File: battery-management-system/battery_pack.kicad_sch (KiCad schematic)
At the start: 16 parts, among them J1 CELL4_PLUS, J2 CELL4_MINUS, J3 CELL3_MINUS, J4 CELL2_MINUS, J5 CELL1_MINUS, J6 VBAT+, J8 VBAT+, Q1 DMN3730U, Q2 TJ40S04M3L, Q3 TJ40S04M3L, Q4 DMN3730U

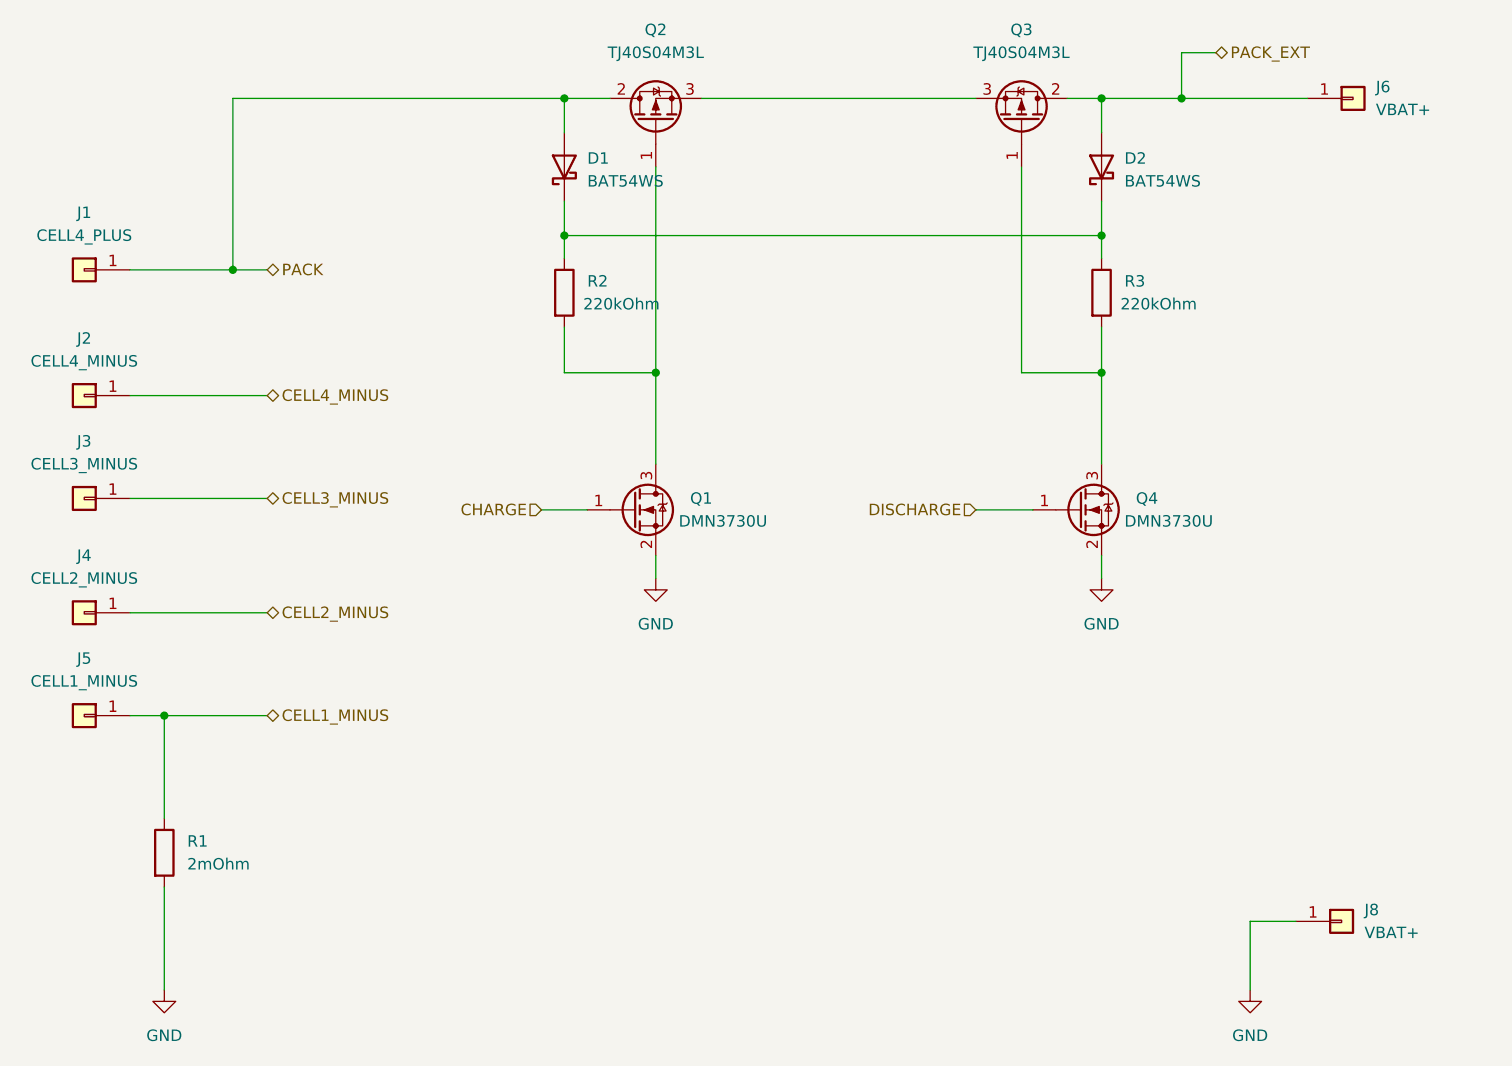
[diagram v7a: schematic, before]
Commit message: add resistors, capacitors and LEDs
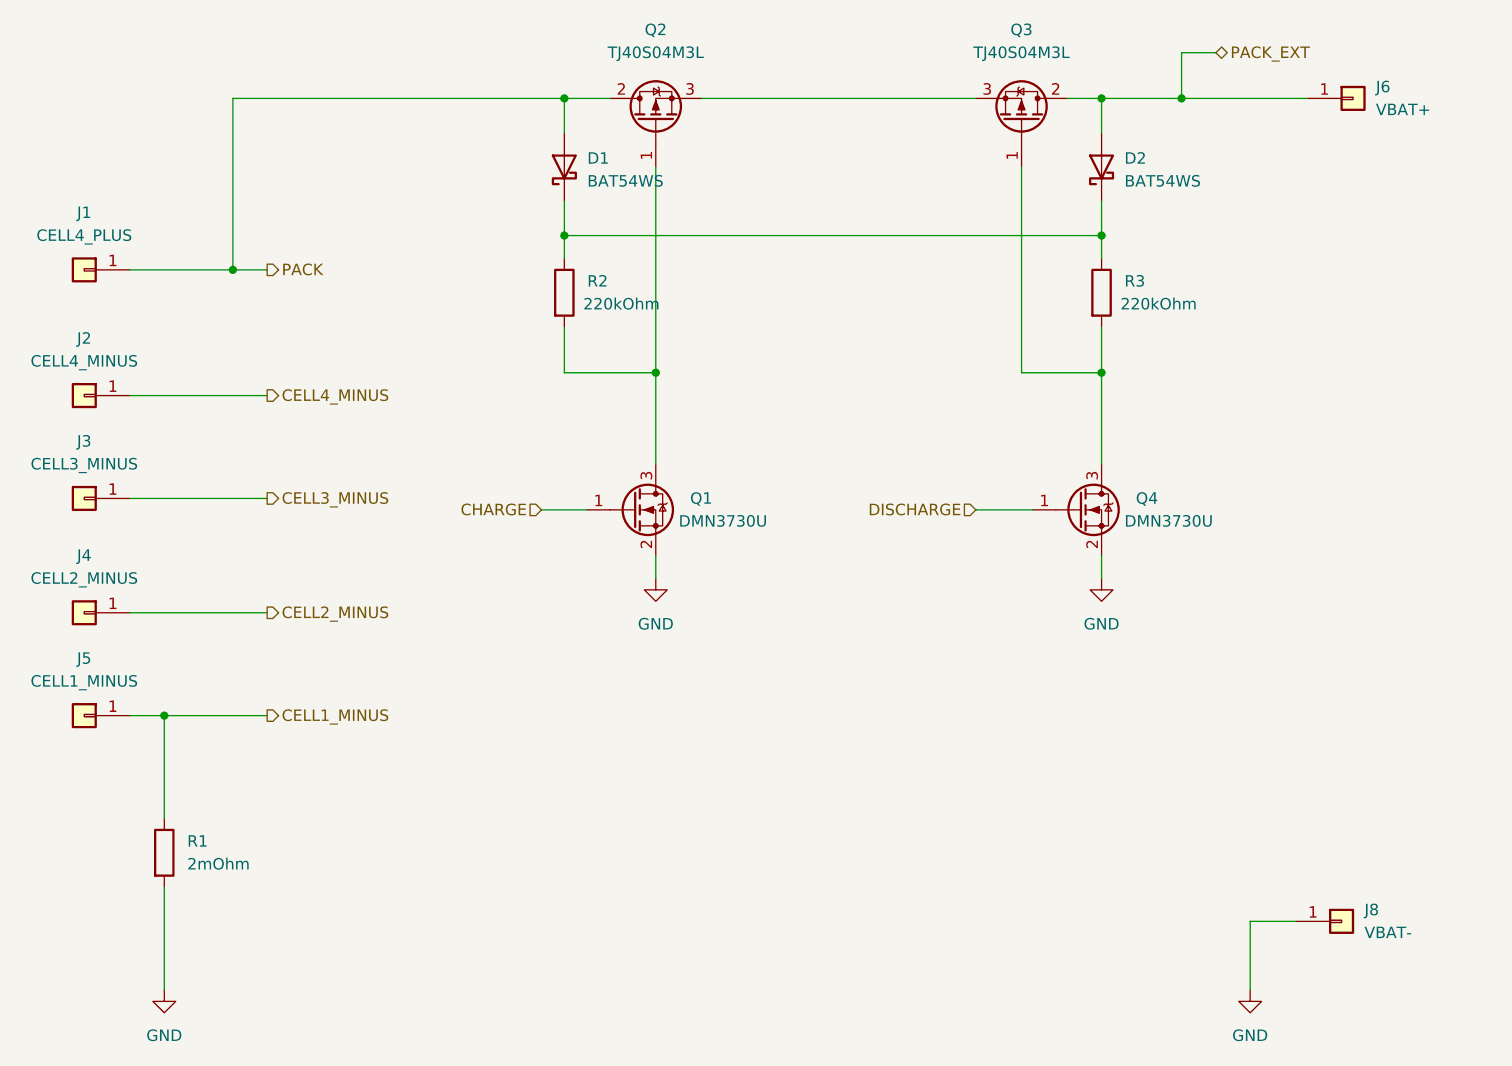
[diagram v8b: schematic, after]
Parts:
- J8: value VBAT+ -> VBAT-
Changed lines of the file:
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@@
     (effects (font (size 1.27 1.27)) (justify right))
   )
-  (hierarchical_label "CELL1_MINUS" (shape bidirectional) (at 86.36 114.3 0)
+  (hierarchical_label "CELL1_MINUS" (shape output) (at 86.36 114.3 0)
     (effects (font (size 1.27 1.27)) (justify left))
   )
-  (hierarchical_label "CELL3_MINUS" (shape bidirectional) (at 86.36 90.17 0)
+  (hierarchical_label "CELL3_MINUS" (shape output) (at 86.36 90.17 0)
     (effects (font (size 1.27 1.27)) (justify left))
   )
-  (hierarchical_label "CELL4_MINUS" (shape bidirectional) (at 86.36 78.74 0)
+  (hierarchical_label "CELL4_MINUS" (shape output) (at 86.36 78.74 0)
     (effects (font (size 1.27 1.27)) (justify left))
   )
-  (hierarchical_label "PACK" (shape bidirectional) (at 86.36 64.77 0)
+  (hierarchical_label "PACK" (shape output) (at 86.36 64.77 0)
     (effects (font (size 1.27 1.27)) (justify left))
   )
@@
     (effects (font (size 1.27 1.27)) (justify left))
   )
-  (hierarchical_label "CELL2_MINUS" (shape bidirectional) (at 86.36 102.87 0)
+  (hierarchical_label "CELL2_MINUS" (shape output) (at 86.36 102.87 0)
     (effects (font (size 1.27 1.27)) (justify left))
   )
@@
       (effects (font (size 1.27 1.27)) (justify left))
     )
-    (property "Value" "VBAT+" (id 1) (at 208.28 138.4299 0)
+    (property "Value" "VBAT-" (id 1) (at 208.28 138.4299 0)
       (effects (font (size 1.27 1.27)) (justify left))
     )
